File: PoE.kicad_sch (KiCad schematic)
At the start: 24 parts, among them IC1 TPS2378DDA

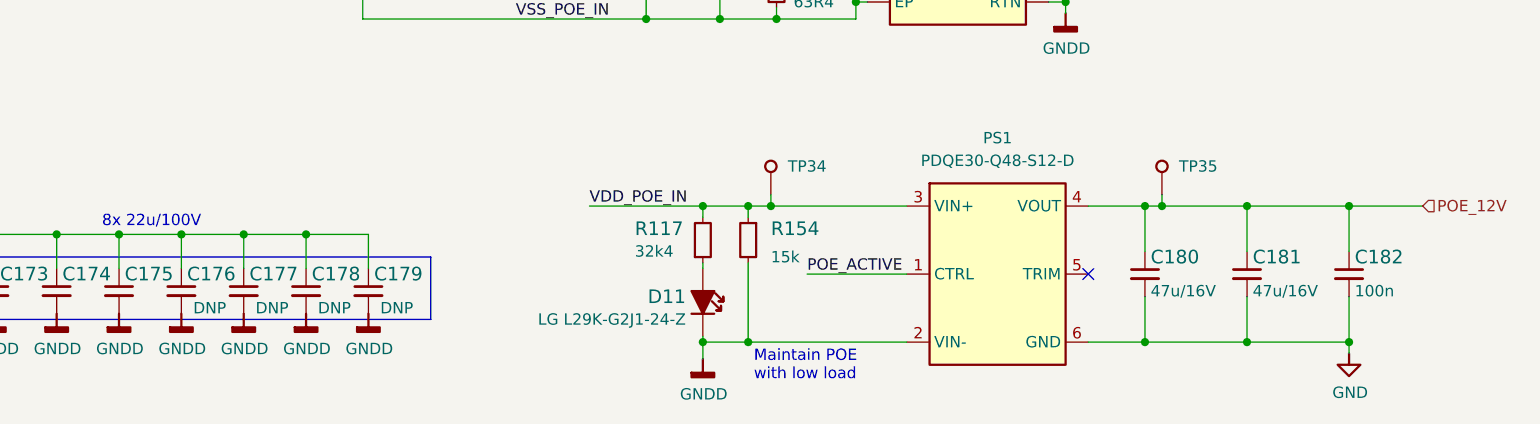
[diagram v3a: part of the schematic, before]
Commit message: [#56935] Update symbol/footprint links; Migrate to KiCad 7
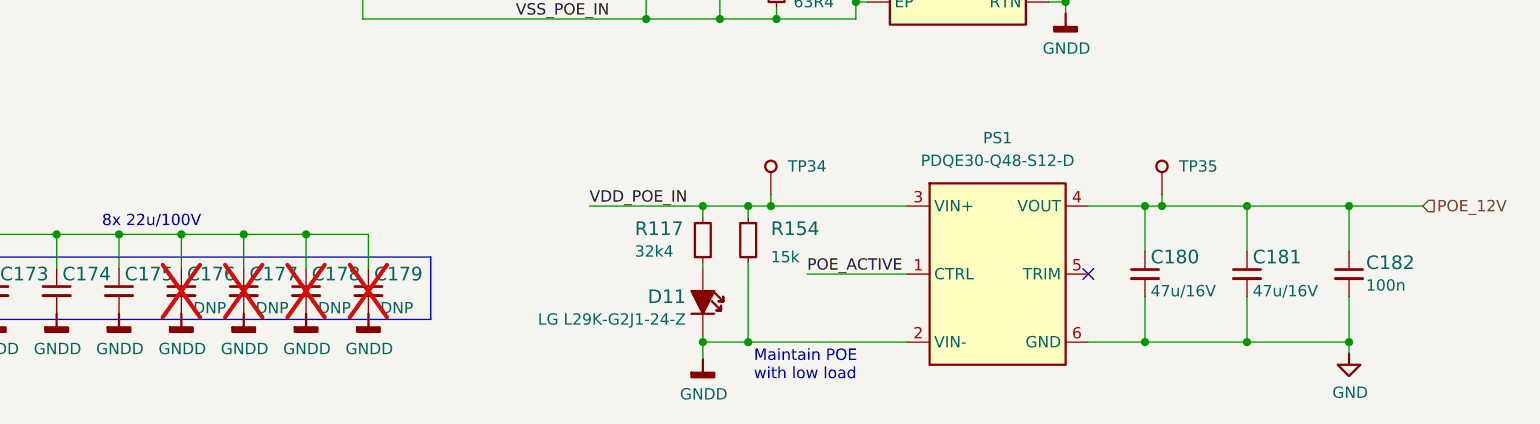
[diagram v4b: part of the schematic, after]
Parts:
- C171: footprint kria-k26-devboard-footprints:C_0805_2012Metric -> antmicro-footprints:C_0805_2012Metric; symbol kria-k26-devboard:C_100n_0805_100V -> antmicroCapacitorsmisc:C_100n_100V_0805
- C172, C173, C174, C175: footprint kria-k26-devboard-footprints:C_2220_5650Metric -> antmicro-footprints:C_2220_5650Metric; symbol kria-k26-devboard:C_22u_100V_2220 -> antmicroCapacitorsmisc:C_22u_100V_2220
- C176, C177, C178, C179: footprint kria-k26-devboard-footprints:C_2220_5650Metric -> antmicro-footprints:C_2220_5650Metric; symbol kria-k26-devboard:C_22u_100V_2220 -> antmicroCapacitorsmisc:C_22u_100V_2220; now not fitted; now left out of the parts list
- C180, C181: footprint kria-k26-devboard-footprints:C_1206_3216Metric -> antmicro-footprints:C_1206_3216Metric; symbol kria-k26-devboard:C_47u_16V_1206 -> antmicroCapacitorsmisc:C_47u_16V_1206
- C182: value C_100n_16V_0402 -> C_100n_0402; footprint kria-k26-devboard-footprints:C_0402_1005Metric -> antmicro-footprints:C_0402_1005Metric; symbol kria-k26-devboard:C_100n_16V_0402 -> antmicroCapacitors0402:C_100n_0402; Dielectric (none) -> X5R; MPN MC0402B104K160CT -> GRM155R61H104KE14D; Manufacturer Multicomp -> Murata; Voltage (none) -> 50V
- D10: footprint kria-k26-devboard-footprints:DO-214AC -> antmicro-footprints:DO-214AC; symbol kria-k26-devboard:SMAJ58A-13-F -> antmicroDiodesRectifiersSingle:SMAJ58A-13-F
- D11: footprint kria-k26-devboard-footprints:LED_0603_1608Metric_G -> antmicro-footprints:LED_0603_1608Metric_G; symbol kria-k26-devboard:LED_G_0603_LG_L29K-G2J1-24-Z -> antmicroLEDIndicationDiscrete:LED_G_0603_LG_L29K-G2J1-24-Z
- D8, D9: footprint kria-k26-devboard-footprints:SOIC-4_4.2x5.0mm_P5.7mm -> antmicro-footprints:SOIC-4_W3.9mm; symbol kria-k26-devboard:MB10S -> antmicroTVSDiodes:MB10S
- IC1: footprint kria-k26-devboard-footprints:SOIC-8-1EP_3.9x4.9x1.75mm_P1.27mm -> antmicro-footprints:SOIC-8-1EP_3.9x4.9x1.75mm_P1.27mm; symbol kria-k26-devboard:TPS2378DDA -> antmicroPMICPowerDistributionSwitchesLoadDrivers:TPS2378DDA
- PS1: footprint kria-k26-devboard-footprints:CONV_PDQE30-Q48-S5-D -> antmicro-footprints:CONV_PDQE30-Q48-S5-D; symbol kria-k26-devboard:PDQE30-Q48-S12-D -> antmicroDCDCConverters:PDQE30-Q48-S12-D
- R115: footprint kria-k26-devboard-footprints:R_0402_1005Metric -> antmicro-footprints:R_0402_1005Metric; symbol kria-k26-devboard:R_24k9_0402 -> antmicroResistors0402:R_24k9_0402
- R116: footprint kria-k26-devboard-footprints:R_0603_1608Metric -> antmicro-footprints:R_0603_1608Metric; symbol kria-k26-devboard:R_63R4_0603 -> antmicroResistors0603:R_63R4_0603
- R117: footprint kria-k26-devboard-footprints:R_0805_2012Metric -> antmicro-footprints:R_0805_2012Metric; symbol kria-k26-devboard:R_32k4_0805 -> antmicroResistorsmisc:R_32k4_0805
- R154: footprint kria-k26-devboard-footprints:R_2010_5025Metric -> antmicro-footprints:R_2010_5025Metric; symbol kria-k26-devboard:R_15k_2010 -> antmicroResistorsmisc:R_15k_2010
- TP34, TP35: footprint kria-k26-devboard-footprints:TP_SMD_0.75mm -> antmicro-footprints:TP_SMD_0.75mm; symbol kria-k26-devboard:TP_0.75mm_SMD -> antmicroTestPoints:TP_0.75mm_SMD

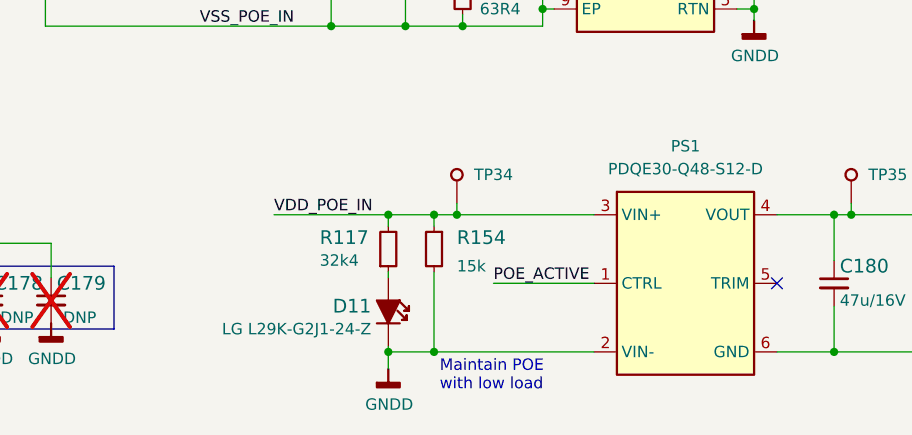
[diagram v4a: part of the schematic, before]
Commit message: [#56935] Fix missing highlights in OHP
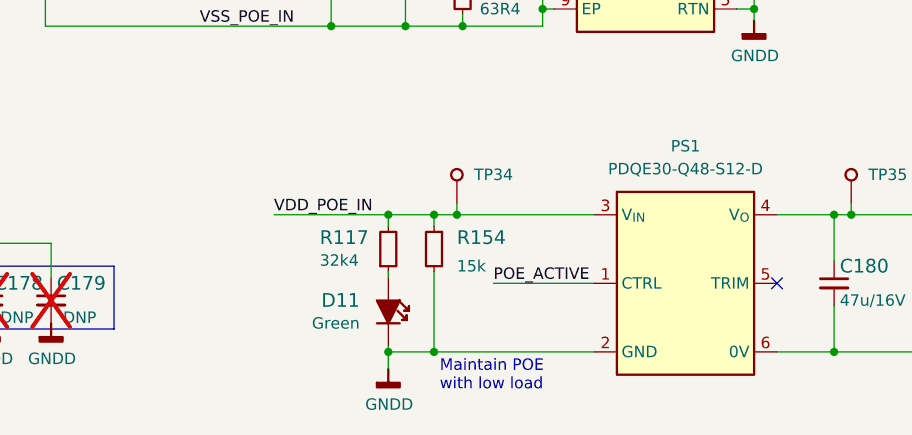
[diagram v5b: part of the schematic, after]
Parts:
- D11: Color (none) -> Green; Manufacturer Osram -> OSRAM
- D8, D9: Manufacturer Multicomp -> Multicomp Pro
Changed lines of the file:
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@@
       (effects (font (size 1.27 1.27) (thickness 0.15)))
     )
-    (property "Manufacturer" "Multicomp" (at 117.475 37.6991 0)
+    (property "Manufacturer" "Multicomp Pro" (at 117.475 37.6991 0)
       (effects (font (size 1.27 1.27) (thickness 0.15)) (justify left bottom) hide)
     )
@@
       (effects (font (size 1.27 1.27) (thickness 0.15)))
     )
-    (property "Manufacturer" "Multicomp" (at 117.475 76.1891 0)
+    (property "Manufacturer" "Multicomp Pro" (at 117.475 76.1891 0)
       (effects (font (size 1.27 1.27) (thickness 0.15)) (justify left bottom) hide)
     )
@@
   )
   (symbol (lib_id "antmicroLEDIndicationDiscrete:LED_G_0603_LG_L29K-G2J1-24-Z") (at 145.415 97.79 270) (unit 1)
-    (in_bom yes) (on_board yes) (dnp no)
-    (property "Reference" "D11" (at 143.51 100.965 90)
+    (in_bom yes) (on_board yes) (dnp no) (fields_autoplaced)
+    (property "Reference" "D11" (at 142.24 100.33 90)
       (effects (font (size 1.524 1.524)) (justify right))
     )
@@
       (effects (font (size 1.27 1.27) (thickness 0.15)) (justify left bottom) hide)
     )
-    (property "MPN" "LG L29K-G2J1-24-Z" (at 143.51 103.505 90)
-      (effects (font (size 1.27 1.27) (thickness 0.15)) (justify right))
-    )
-    (property "Manufacturer" "Osram" (at 173.355 102.87 0)
+    (property "MPN" "LG L29K-G2J1-24-Z" (at 143.51 103.505 0)
+      (effects (font (size 1.27 1.27) (thickness 0.15)) (justify left bottom) hide)
+    )
+    (property "Manufacturer" "OSRAM" (at 173.355 102.87 0)
       (effects (font (size 1.27 1.27) (thickness 0.15)) (justify left bottom) hide)
     )
@@
       (effects (font (size 1.27 1.27) (thickness 0.15)) (justify left bottom) hide)
     )
-    (pin "1")
+    (property "Color" "Green" (at 142.24 102.87 90)
+      (effects (font (size 1.27 1.27)) (justify right))
+    )
+    (pin "1")

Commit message: [#56935] Loclib
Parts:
- C171: footprint antmicro-footprints:C_0805_2012Metric -> kria-k26-devboard-footprints:C_0805_2012Metric; symbol antmicroCapacitorsmisc:C_100n_100V_0805 -> kria-k26-devboard:C_100n_100V_0805
- C172, C173, C174, C175, C176, C177, C178, C179: footprint antmicro-footprints:C_2220_5650Metric -> kria-k26-devboard-footprints:C_2220_5650Metric; symbol antmicroCapacitorsmisc:C_22u_100V_2220 -> kria-k26-devboard:C_22u_100V_2220
- C180, C181: footprint antmicro-footprints:C_1206_3216Metric -> kria-k26-devboard-footprints:C_1206_3216Metric; symbol antmicroCapacitorsmisc:C_47u_16V_1206 -> kria-k26-devboard:C_47u_16V_1206
- C182: footprint antmicro-footprints:C_0402_1005Metric -> kria-k26-devboard-footprints:C_0402_1005Metric; symbol antmicroCapacitors0402:C_100n_0402 -> kria-k26-devboard:C_100n_0402
- D10: footprint antmicro-footprints:DO-214AC -> kria-k26-devboard-footprints:DO-214AC; symbol antmicroDiodesRectifiersSingle:SMAJ58A-13-F -> kria-k26-devboard:SMAJ58A-13-F
- D11: footprint antmicro-footprints:LED_0603_1608Metric_G -> kria-k26-devboard-footprints:LED_0603_1608Metric_G; symbol antmicroLEDIndicationDiscrete:LED_G_0603_LG_L29K-G2J1-24-Z -> kria-k26-devboard:LED_G_0603_LG_L29K-G2J1-24-Z
- D8, D9: footprint antmicro-footprints:SOIC-4_W3.9mm -> kria-k26-devboard-footprints:SOIC-4_W3.9mm; symbol antmicroTVSDiodes:MB10S -> kria-k26-devboard:MB10S
- IC1: footprint antmicro-footprints:SOIC-8-1EP_3.9x4.9x1.75mm_P1.27mm -> kria-k26-devboard-footprints:SOIC-8-1EP_3.9x4.9x1.75mm_P1.27mm; symbol antmicroPMICPowerDistributionSwitchesLoadDrivers:TPS2378DDA -> kria-k26-devboard:TPS2378DDA
- PS1: footprint antmicro-footprints:CONV_PDQE30-Q48-S5-D -> kria-k26-devboard-footprints:CONV_PDQE30-Q48-S5-D; symbol antmicroDCDCConverters:PDQE30-Q48-S12-D -> kria-k26-devboard:PDQE30-Q48-S12-D
- R115: footprint antmicro-footprints:R_0402_1005Metric -> kria-k26-devboard-footprints:R_0402_1005Metric; symbol antmicroResistors0402:R_24k9_0402 -> kria-k26-devboard:R_24k9_0402
- R116: footprint antmicro-footprints:R_0603_1608Metric -> kria-k26-devboard-footprints:R_0603_1608Metric; symbol antmicroResistors0603:R_63R4_0603 -> kria-k26-devboard:R_63R4_0603
- R117: footprint antmicro-footprints:R_0805_2012Metric -> kria-k26-devboard-footprints:R_0805_2012Metric; symbol antmicroResistorsmisc:R_32k4_0805 -> kria-k26-devboard:R_32k4_0805
- R154: footprint antmicro-footprints:R_2010_5025Metric -> kria-k26-devboard-footprints:R_2010_5025Metric; symbol antmicroResistorsmisc:R_15k_2010 -> kria-k26-devboard:R_15k_2010
- TP34, TP35: footprint antmicro-footprints:TP_SMD_0.75mm -> kria-k26-devboard-footprints:TP_SMD_0.75mm; symbol antmicroTestPoints:TP_0.75mm_SMD -> kria-k26-devboard:TP_0.75mm_SMD
